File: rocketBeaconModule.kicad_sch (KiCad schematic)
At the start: 42 parts, among them J1 TYPE-C-31-M-12, J2 PWR, J3 GND, J4 PWR, J5 GND, U1 STM32F401CCU6, U2 CP2102N-Axx-xQFN20, Y1 16MHz

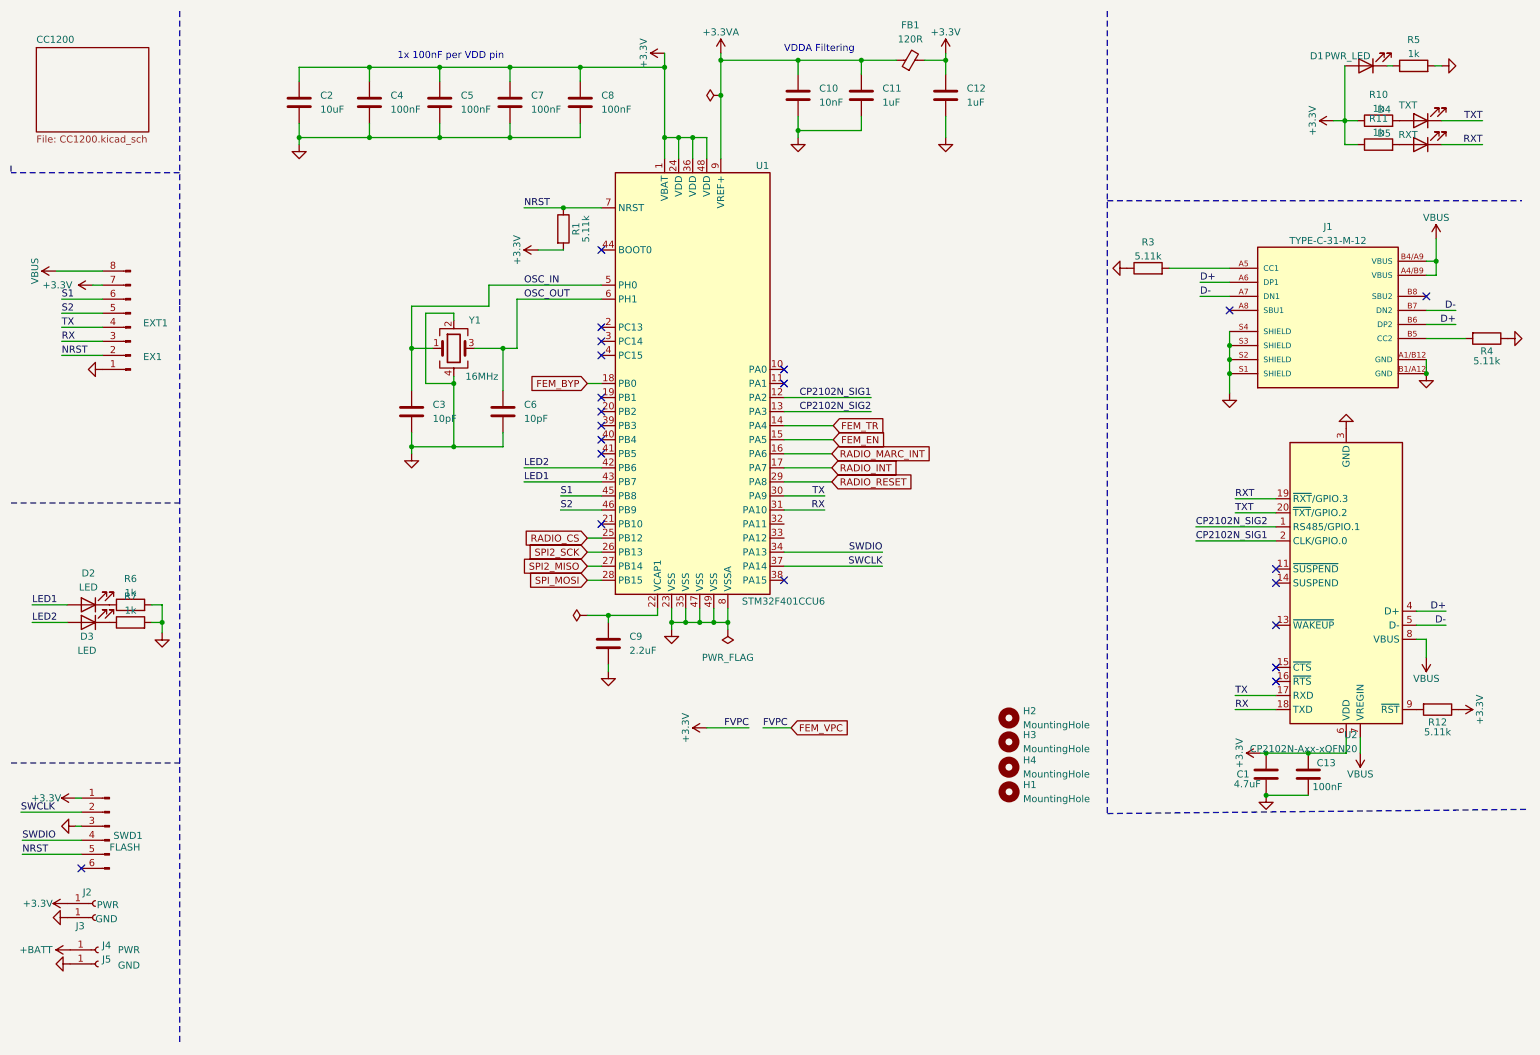
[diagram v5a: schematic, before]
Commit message: added Mitsibushi Amp w/ supporting gate control circuitry, switching, and temperature monitoring
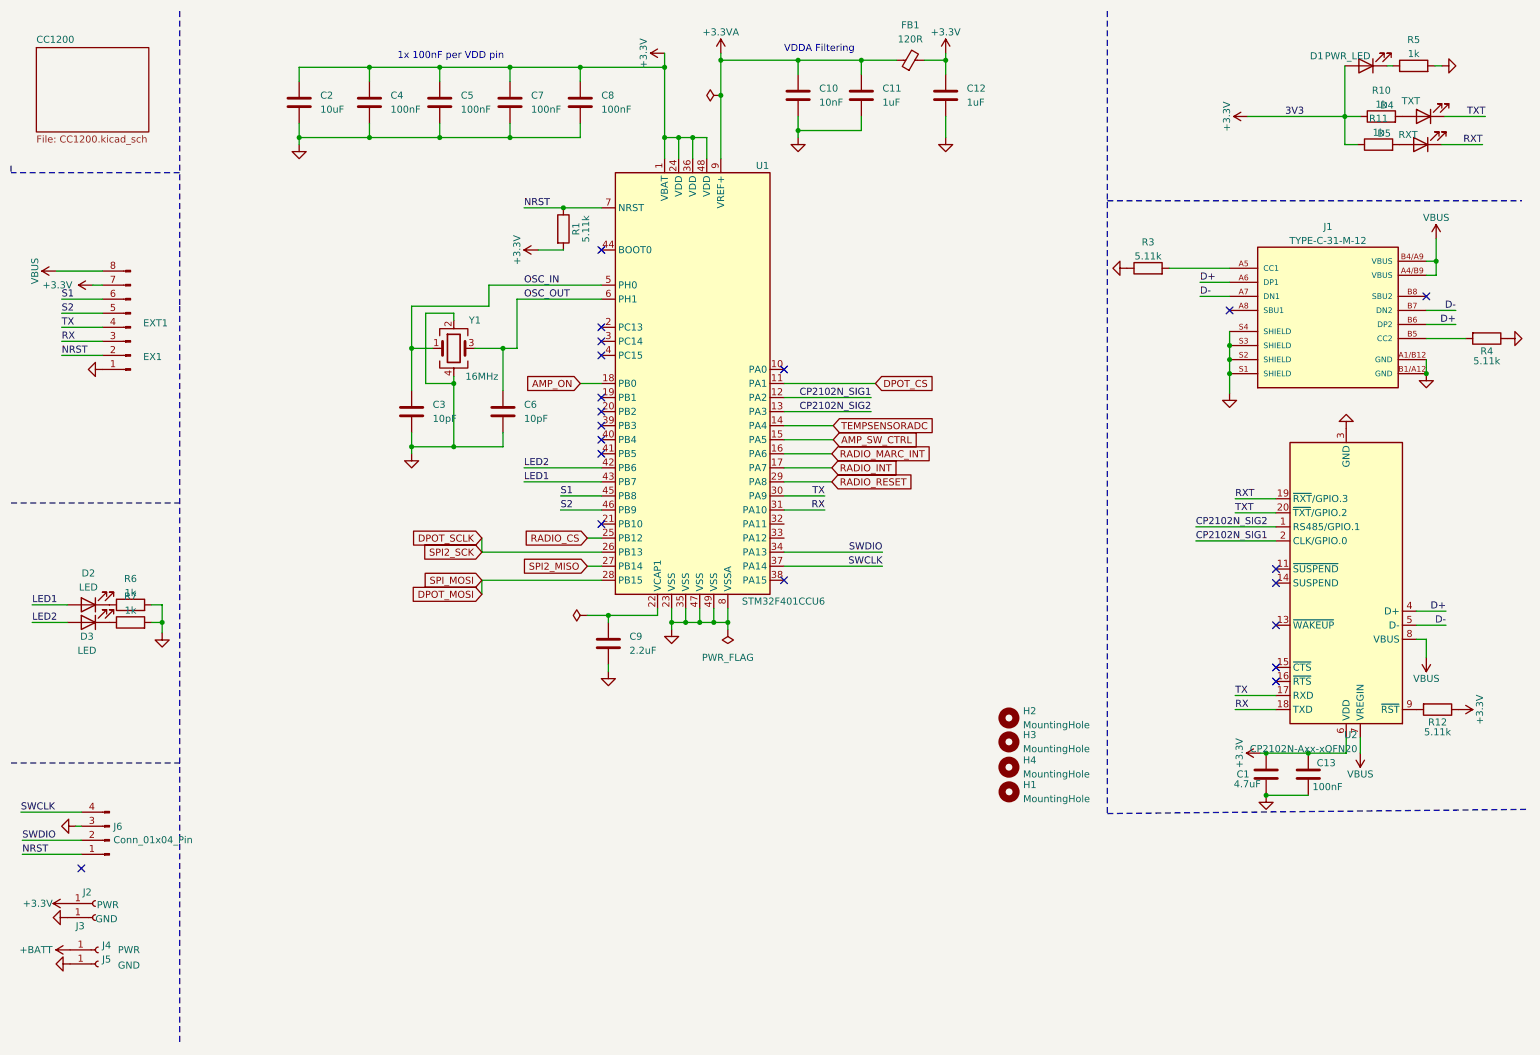
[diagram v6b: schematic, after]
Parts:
- removed SWD1: FLASH, Connector_PinSocket_2.54mm:PinSocket_1x05_P2.54mm_Vertical, symbol Connector:Conn_01x06_Male
- added J6: Conn_01x04_Pin, Connector_PinHeader_2.54mm:PinHeader_1x04_P2.54mm_Vertical, symbol Connector:Conn_01x04_Pin
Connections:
- net GND: now also J6.3 (Pin_3)
- net NRST: now also J6.1 (Pin_1)
- net SWCLK: now also J6.4 (Pin_4)
- net SWDIO: now also J6.2 (Pin_2)
- net DPOT_CS: now reaches U1.11 (PA1)
- net FEM_BYP renamed AMP_ON
- net FEM_EN renamed AMP_SW_CTRL
- net FEM_TR renamed TEMPSENSORADC
- net SPI2_SCK renamed DPOT_SCLK
- net SPI_MOSI renamed DPOT_MOSI
- no-connect marks 21 -> 20
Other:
- moved on the sheet: D4, R10

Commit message: BOM fixes and manufactureing files
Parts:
- C2: LCSC Part c -> C19702
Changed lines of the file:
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@@
 			)
 		)
-		(property "LCSC Part" "c"
+		(property "LCSC Part" "C19702"
 			(at 63.5 27.94 0)
 			(effects
